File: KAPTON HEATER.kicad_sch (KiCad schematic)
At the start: 29 parts, among them J1 Conector, Q2 NTMFS4C10N

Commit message: Kapton
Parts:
- removed CF1: C, footprints:Cf, symbol Device:C
- removed Cin1: C, footprints:Cin, symbol Device:C
- removed Cout1: C, footprints:Cout, symbol Device:C
- removed R1: CRE2512-FZ-R003E-3, footprints:PFET Resistor, symbol Kapton PCB:CRE2512-FZ-R003E-3
- removed U1: ~, footprints:PFET, symbol Kapton PCB:PFET
- removed U3: ~, footprints:SOIC-8, symbol Kapton PCB:LP2975
- removed U5: ~, symbol Kapton PCB:24V_INPUT
- added J1: Screw_Terminal_01x04, symbol Connector:Screw_Terminal_01x04
- added U1: L7805, symbol Regulator_Linear:L7805
- F1: value Fuse -> Fast-blow
- F2: value Fuse -> Slow blow
- R2, R3, R4, R5: value R -> 6.8k
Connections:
- net GND: now reaches J1.4, Q2.1~3 (S), R2.2, R3.2, R4.2, R5.2, U8.4 (N/C)
- net GND: now also J1.2 (Pin_2), U1.2 (GND)
- net 5V: now reaches TH1.1, TH2.1, TH3.1, TH4.1
- net 5V: no longer U6. (3.3V)
- net 24V 14.6A: now reaches U2., U8.5
- net 24V 14.6A: now also J1.1 (Pin_1), U1.1 (IN)
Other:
- note added: "Pin 4 to receive PWM from MCU."
- note added: "Pin is to receive switching signal from MCU."
- note removed: "To be recieved from PWM pin on MCU."
- company: (none) -> QRET
- title: (none) -> May 22nd Update
- moved on the sheet: F1, F2, J1, Q2, R2, R3, R4, R5, TH1, TH2, TH3, TH4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

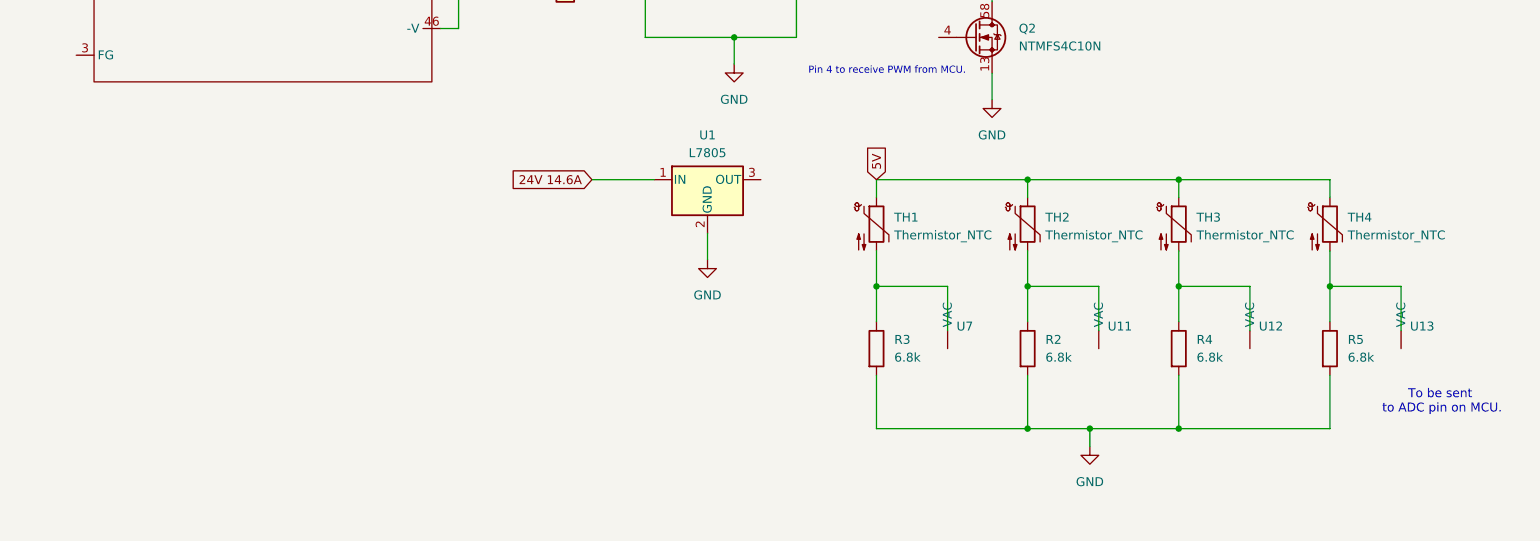
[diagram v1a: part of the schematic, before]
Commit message: Commit 3
Connection from rigid to flex sections added. 12 Pin connector for thermistor signal(s) and power.
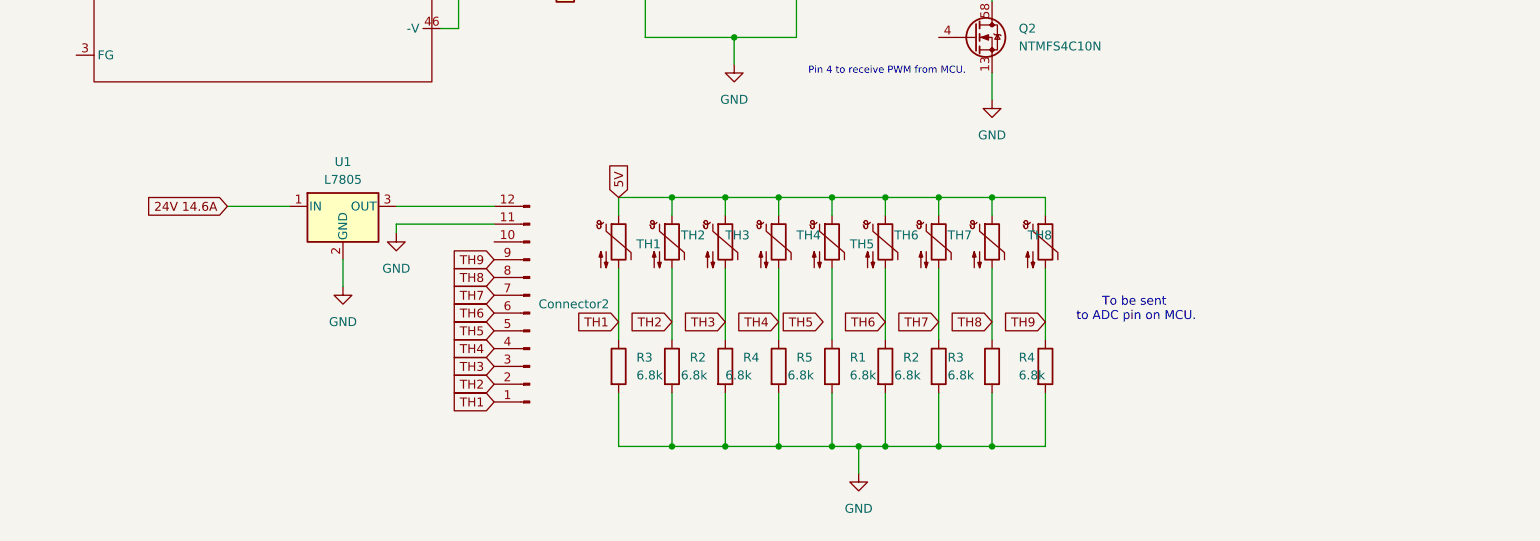
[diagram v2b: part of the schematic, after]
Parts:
- removed U11, U12, U13, U7: ~, symbol Kapton PCB:Thermisistor_Vout
- added Connector2: Conn_01x12_Pin, symbol Connector:Conn_01x12_Pin
- added R1, R2, R3, R4, R5: 6.8k, footprints:Thermistor Resistors, symbol Device:R
- added TH5, TH6, TH7, TH8, TH9: Thermistor_NTC, footprints:Thermistor, symbol Device:Thermistor_NTC
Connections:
- net 5V: now also TH5.1, TH6.1, TH7.1, TH8.1, TH9.1
- net GND: now also Connector2.11 (Pin_11), R1.2, R2.2, R3.2, R4.2, R5.2
- net TH4: now reaches R5.1, TH4.2
- net TH4: now also Connector2.4 (Pin_4)
- net TH2: now reaches R2.1, TH2.2
- net TH2: now also Connector2.2 (Pin_2)
- net TH1: now reaches R3.1, TH1.2
- net TH1: now also Connector2.1 (Pin_1)
- net TH3: now reaches R4.1, TH3.2
- net TH3: now also Connector2.3 (Pin_3)
- net at U1.3 (OUT): now also Connector2.12 (Pin_12)
- new net: R1.1, TH5.2
- new net TH5: Connector2.5 (Pin_5)
- new net TH6: Connector2.6 (Pin_6), R2.1, TH6.2
- new net TH7: Connector2.7 (Pin_7), R3.1, TH7.2
- new net TH8: Connector2.8 (Pin_8), R4.1, TH8.2
- new net TH9: Connector2.9 (Pin_9), R5.1, TH9.2
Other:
- moved on the sheet: R2, R3, R4, R5, TH1, TH2, TH3, TH4, U1

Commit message: Commit 3.1
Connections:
- net 5V: now also Connector2.12 (Pin_12), U1.3 (OUT)
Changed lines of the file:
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@@
+		)
+	)
+	(global_label "5V"
+		(shape input)
+		(at 114.3 110.49 90)
+		(fields_autoplaced yes)
+		(effects
+			(font
+				(size 1.27 1.27)
+			)
+			(justify left)
+		)
+		(property "Intersheetrefs" "${INTERSHEET_REFS}"
+			(at 114.3 105.2067 90)
+			(effects
+				(font
+					(size 1.27 1.27)
+				)
+				(justify left)
+				(hide yes)
+			)
 		)
 	)

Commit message: Commit 3.2
Floated GND
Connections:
- net GND: no longer U1.2 (GND)
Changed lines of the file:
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@@
-	(wire
-		(pts
-			(xy 99.06 118.11) (xy 99.06 121.92)
-		)
-		(stroke
-			(width 0)
-			(type default)
-		)
-	)
 	(wire
 		(pts
@@
 					(unit 1)
 				)
-			)
-		)
-	)
-	(symbol
-		(lib_id "power:GND")
-		(at 99.06 121.92 0)
-		(unit 1)
-		(exclude_from_sim no)
-		(in_bom yes)
-		(on_board yes)
-		(dnp no)
-		(fields_autoplaced yes)
-		(property "Reference" "#PWR05"
-			(at 99.06 128.27 0)
-			(effects
-				(font
-					(size 1.27 1.27)
-				)
-				(hide yes)
-			)
-		)
-		(property "Value" "GND"
-			(at 99.06 127 0)
-			(effects
-				(font
-					(size 1.27 1.27)
-				)
-			)
-		)
-		(property "Footprint" ""
-			(at 99.06 121.92 0)
-			(effects
-				(font
-					(size 1.27 1.27)
-				)
-				(hide yes)
-			)
-		)
-		(property "Datasheet" ""
-			(at 99.06 121.92 0)
-			(effects
-				(font
-					(size 1.27 1.27)
-				)
-				(hide yes)
-			)
-		)
-		(property "Description" "Power symbol creates a global label with name \"GND\" , ground"
-			(at 99.06 121.92 0)
-			(effects
-				(font
-					(size 1.27 1.27)
-				)
-				(hide yes)
-			)
-		)
-		(pin "1"
-		)
-		(instances
-			(project "KAPTON HEATER"
-				(path "/7feaf6fb-b480-44b3-9b98-6bc535f879b3"
-					(reference "#PWR05")
-					(unit 1)
-				)
